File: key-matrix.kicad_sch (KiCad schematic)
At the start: 176 parts

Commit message: first draft
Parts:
- K14: renamed from K?; value BACKTICK -> BCKTCK
- K28: renamed from K?; value PRT_SC -> PRNT
- K29: renamed from K?; value SCR_LK -> SCRL
- K74: renamed from K?; value FLLSTP -> DOT
- gave numbers to parts that had none: 172

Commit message: more tweaks
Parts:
- renumbered D9 to D10, D10 to D11, D11 to D12, D12 to D13, D13 to D14, D14 to D15, D15 to D16, D16 to D17, D17 to D18, D18 to D19, D1 to D2, D19 to D20, D20 to D21, D21 to D22, D22 to D23, D23 to D24, D24 to D25, D25 to D26, D26 to D27, D27 to D28, D28 to D29, D2 to D3, D29 to D30, D30 to D31, D31 to D32, D32 to D33, D33 to D34, D34 to D35, D35 to D36, D36 to D37, D37 to D38, D38 to D39, D3 to D4, D39 to D40, D40 to D41, D41 to D42, D42 to D43, D43 to D44, D44 to D45, D45 to D46, D46 to D47, D47 to D48, D48 to D49, D4 to D5, D49 to D50, D50 to D51, D51 to D52, D52 to D53, D53 to D54, D54 to D55, D55 to D56, D56 to D57, D57 to D58, D58 to D59, D5 to D6, D59 to D60, D60 to D61, D61 to D62, D62 to D63, D63 to D64, D64 to D65, D65 to D66, D66 to D67, D67 to D68, D68 to D69, D6 to D7, D69 to D70, D70 to D71, D71 to D72, D72 to D73, D73 to D74, D74 to D75, D75 to D76, D76 to D77, D77 to D78, D78 to D79, D7 to D8, D79 to D80, D80 to D81, D81 to D82, D82 to D83, D83 to D84, D84 to D85, D85 to D86, D86 to D87, D87 to D88, D88 to D89, D8 to D9

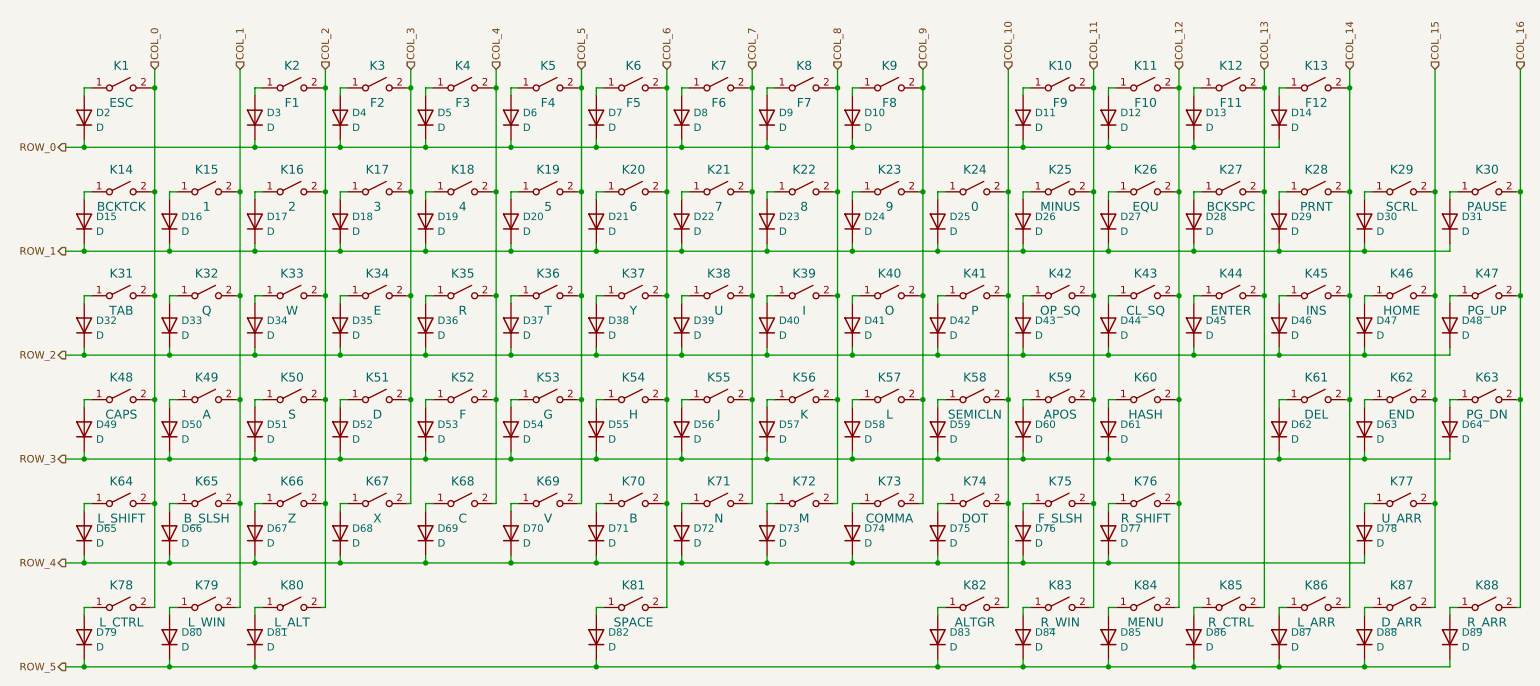
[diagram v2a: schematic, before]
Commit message: keyswitch placement
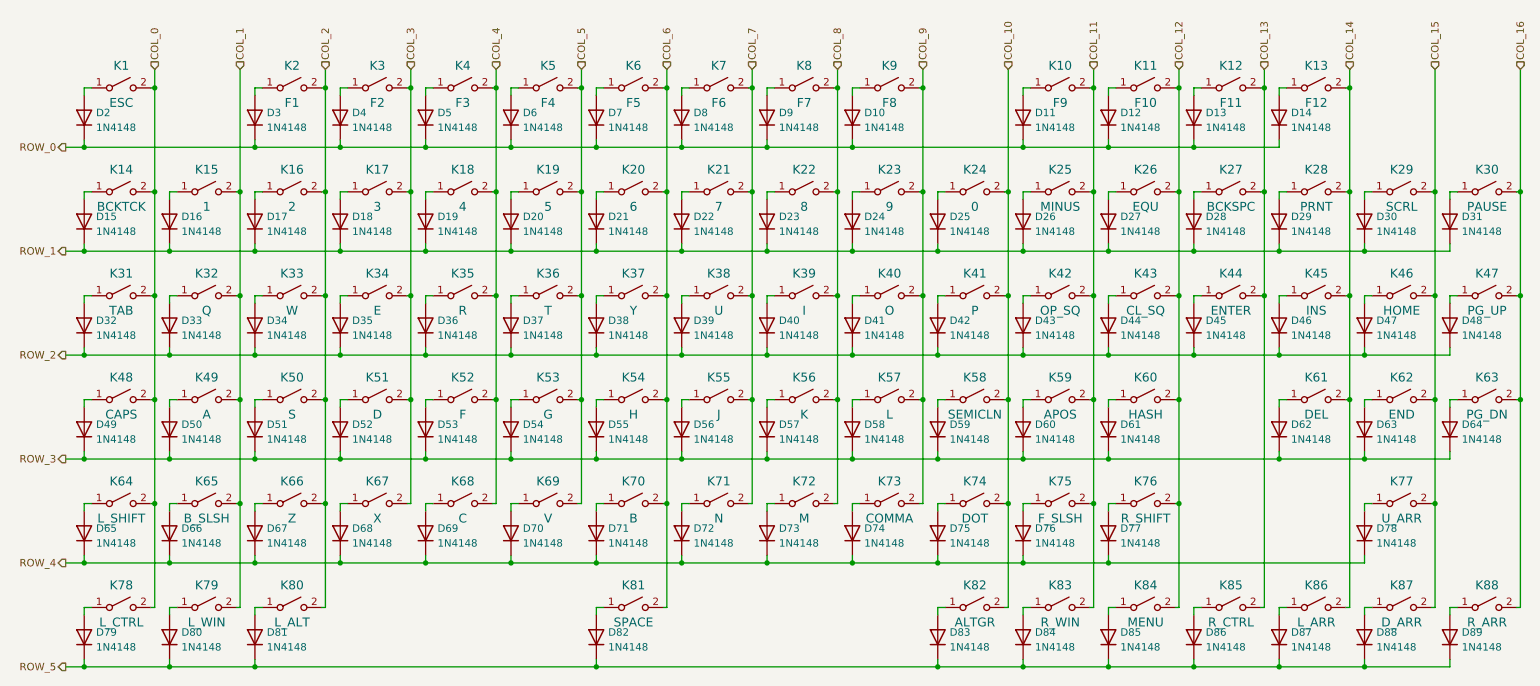
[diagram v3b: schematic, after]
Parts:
- D10, D11, D12, D13, D14, D15, D16, D17, D18, D19, D2, D20, D21, D22, D23, D24, D25, D26, D27, D28, D29, D3, D30, D31, D32, D33, D34, D35, D36, D37, D38, D39, D4, D40, D41, D42, D43, D44, D45, D46, D47, D48, D49, D5, D50, D51, D52, D53, D54, D55, D56, D57, D58, D59, D6, D60, D61, D62, D63, D64, D65, D66, D67, D68, D69, D7, D70, D71, D72, D73, D74, D75, D76, D77, D78, D79, D8, D80, D81, D82, D83, D84, D85, D86, D87, D88, D89, D9: value D -> 1N4148; footprint (none) -> Diode_SMD:D_SOD-123
- K1, K10, K11, K12, K13, K14, K15, K16, K17, K18, K19, K2, K20, K21, K22, K23, K24, K25, K26, K27, K28, K29, K3, K30, K31, K32, K33, K34, K35, K36, K37, K38, K39, K4, K40, K41, K42, K43, K44, K45, K46, K47, K48, K49, K5, K50, K51, K52, K53, K54, K55, K56, K57, K58, K59, K6, K60, K61, K62, K63, K64, K65, K66, K67, K68, K69, K7, K70, K71, K72, K73, K74, K75, K76, K77, K78, K79, K8, K80, K81, K82, K83, K84, K85, K86, K87, K88, K9: footprint (none) -> Custom:SW_Cherry_MX_1.00u_PCB
